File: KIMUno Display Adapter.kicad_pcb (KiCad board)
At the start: 2 copper layers, 66 x 31.8 mm, 3 parts, among them J1 ALS318A

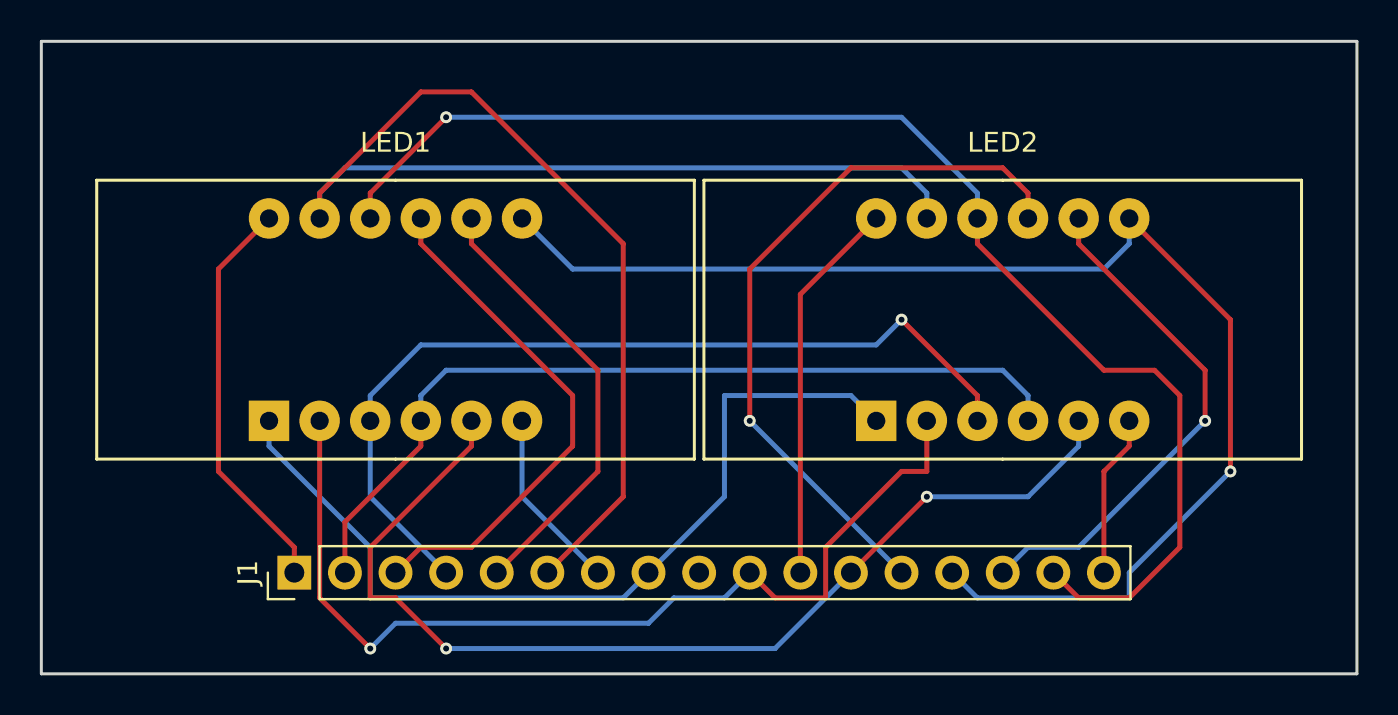
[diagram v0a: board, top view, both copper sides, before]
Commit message: Rev. 00 - Size adjustment
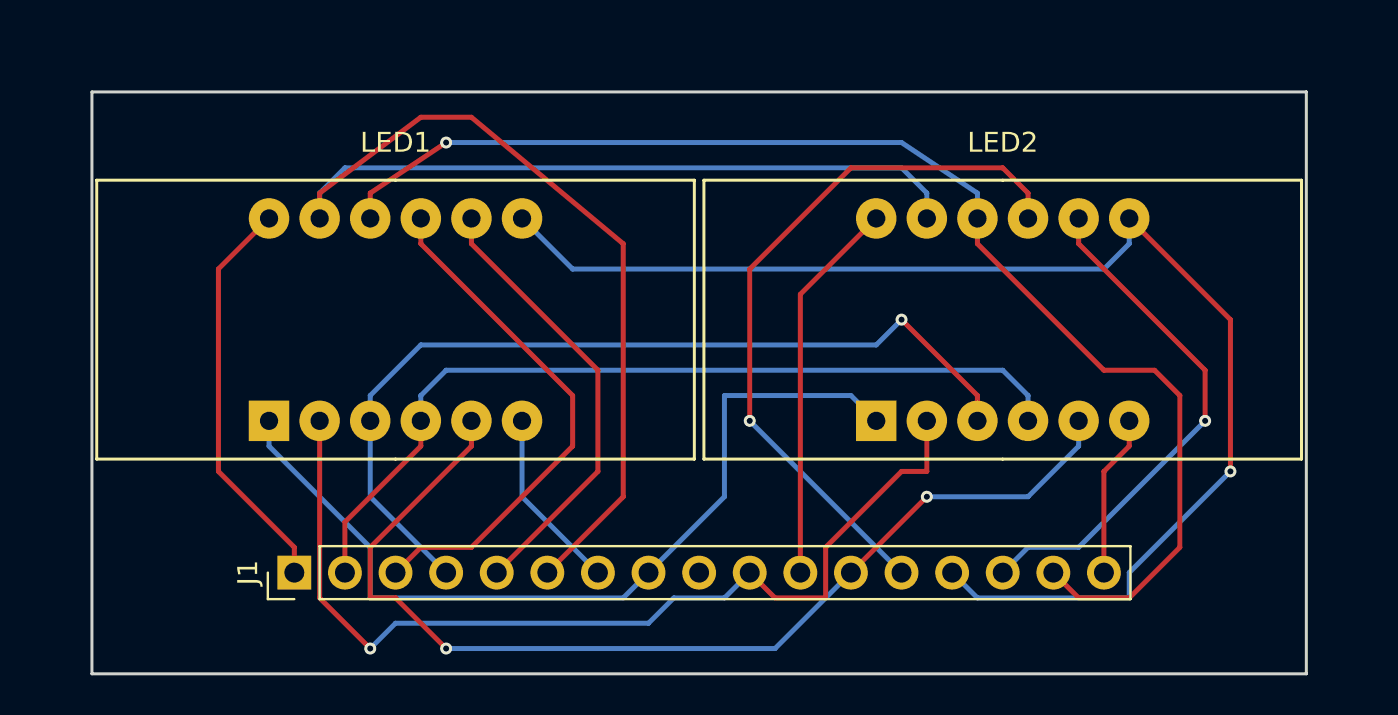
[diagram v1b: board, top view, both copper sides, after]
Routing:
- net /Seg_a: track 73.9 -> 72.2 mm
- net /Seg_f: track 66.3 -> 64.7 mm
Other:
- board size 66 x 31.8 mm -> 61 x 29.2 mm
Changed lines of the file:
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@@
     (links 24)
     (no_connects 0)
-    (area 68.504999 53.264999 134.695001 85.165001)
+    (area 68.504999 53.264999 134.695001 85.17)
     (thickness 1.6)
     (drawings 7)
@@
       (net 13 /CC7))
   )
-  (gr_text "Rev. 00 / 2018-07-23" (at 119.38 83.82) (layer B.SilkS)
+  (gr_line (start 132.08 55.88) (end 132.08 85.09) (angle 90) (layer Edge.Cuts) (width 0.15))
+  (gr_line (start 71.12 55.88) (end 71.12 85.09) (angle 90) (layer Edge.Cuts) (width 0.15))
+  (gr_line (start 71.12 55.88) (end 132.08 55.88) (angle 90) (layer Edge.Cuts) (width 0.15))
+  (gr_line (start 132.08 85.09) (end 71.12 85.09) (angle 90) (layer Edge.Cuts) (width 0.15))
+  (gr_text "Rev. 00 / 2018-07-23" (at 116.84 83.82) (layer B.SilkS)
     (effects (font (size 1.5 1.5) (thickness 0.3)) (justify mirror))
   )
-  (gr_text "Adapter board for ALS318A CC display\nto 2x3461AS for KIM Uno" (at 132.08 67.31) (layer B.SilkS)
+  (gr_text "Adapter board for ALS318A CC display\nto 2x3461AS for KIM Uno" (at 130.81 67.31) (layer B.SilkS)
     (effects (font (size 1.5 1.5) (thickness 0.25)) (justify left mirror))
   )
-  (gr_text "(c) 2018 VintageProject" (at 106.68 55.88) (layer B.SilkS)
+  (gr_text "(c) 2018 VintageProject" (at 104.14 58.42) (layer B.SilkS)
     (effects (font (size 1.5 1.5) (thickness 0.3)) (justify right mirror))
   )
-  (gr_line (start 68.58 85.09) (end 68.58 53.34) (angle 90) (layer Edge.Cuts) (width 0.15))
-  (gr_line (start 134.62 53.34) (end 134.62 85.09) (angle 90) (layer Edge.Cuts) (width 0.15))
-  (gr_line (start 134.62 85.09) (end 68.58 85.09) (angle 90) (layer Edge.Cuts) (width 0.15))
-  (gr_line (start 68.58 53.34) (end 134.62 53.34) (angle 90) (layer Edge.Cuts) (width 0.15))
   (segment (start 80.01 62.23) (end 77.47 64.77) (width 0.25) (layer F.Cu) (net 1) (status 80000))
   (segment (start 77.47 64.77) (end 77.47 74.93) (width 0.25) (layer F.Cu) (net 1) (status 80000))
@@
   (segment (start 96.52 74.93) (end 91.44 80.01) (width 0.25) (layer F.Cu) (net 5) (status 80000))
   (segment (start 82.55 62.23) (end 82.55 60.96) (width 0.25) (layer F.Cu) (net 6) (status 80000))
-  (segment (start 82.55 60.96) (end 87.63 55.88) (width 0.25) (layer F.Cu) (net 6) (status 80000))
-  (segment (start 87.63 55.88) (end 90.17 55.88) (width 0.25) (layer F.Cu) (net 6) (status 80000))
-  (segment (start 90.17 55.88) (end 97.79 63.5) (width 0.25) (layer F.Cu) (net 6) (status 80000))
+  (segment (start 82.55 60.96) (end 87.63 57.15) (width 0.25) (layer F.Cu) (net 6) (status 80000))
+  (segment (start 87.63 57.15) (end 90.17 57.15) (width 0.25) (layer F.Cu) (net 6) (status 80000))
+  (segment (start 90.17 57.15) (end 97.79 63.5) (width 0.25) (layer F.Cu) (net 6) (status 80000))
   (segment (start 97.79 63.5) (end 97.79 76.2) (width 0.25) (layer F.Cu) (net 6) (status 80000))
   (segment (start 97.79 76.2) (end 93.98 80.01) (width 0.25) (layer F.Cu) (net 6) (status 80000))
@@
   (segment (start 115.57 63.5) (end 115.57 62.23) (width 0.25) (layer F.Cu) (net 16) (status 80000))
   (segment (start 115.57 62.23) (end 115.57 60.96) (width 0.25) (layer B.Cu) (net 16) (status 80000))
-  (segment (start 115.57 60.96) (end 111.76 57.15) (width 0.25) (layer B.Cu) (net 16) (status 80000))
-  (segment (start 111.76 57.15) (end 88.9 57.15) (width 0.25) (layer B.Cu) (net 16) (status 80000))
-  (via (at 88.9 57.15) (size 0.6) (layers F.Cu B.Cu) (net 16) (status 80000))
-  (segment (start 88.9 57.15) (end 85.09 60.96) (width 0.25) (layer F.Cu) (net 16) (status 80000))
+  (segment (start 115.57 60.96) (end 111.76 58.42) (width 0.25) (layer B.Cu) (net 16) (status 80000))
+  (segment (start 111.76 58.42) (end 88.9 58.42) (width 0.25) (layer B.Cu) (net 16) (status 80000))
+  (via (at 88.9 58.42) (size 0.6) (layers F.Cu B.Cu) (net 16) (status 80000))
+  (segment (start 88.9 58.42) (end 85.09 60.96) (width 0.25) (layer F.Cu) (net 16) (status 80000))
   (segment (start 85.09 60.96) (end 85.09 62.23) (width 0.25) (layer F.Cu) (net 16) (status 80000))
   (segment (start 123.19 72.39) (end 123.19 73.66) (width 0.25) (layer F.Cu) (net 17) (status 80000))
